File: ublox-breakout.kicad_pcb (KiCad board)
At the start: 4 copper layers, 47.2 x 33.2 mm, 41 parts, among them J1 Conn_02x06_Odd_Even, J2 Conn_Coaxial, J3 Conn_Coaxial, J4 USB_B_Micro, U1 74HCT2G125DP,125, U2 UBLOX_LEA-M8T-0, U3 TPUSBLC6-2SC6, U4 XC6206P332MR

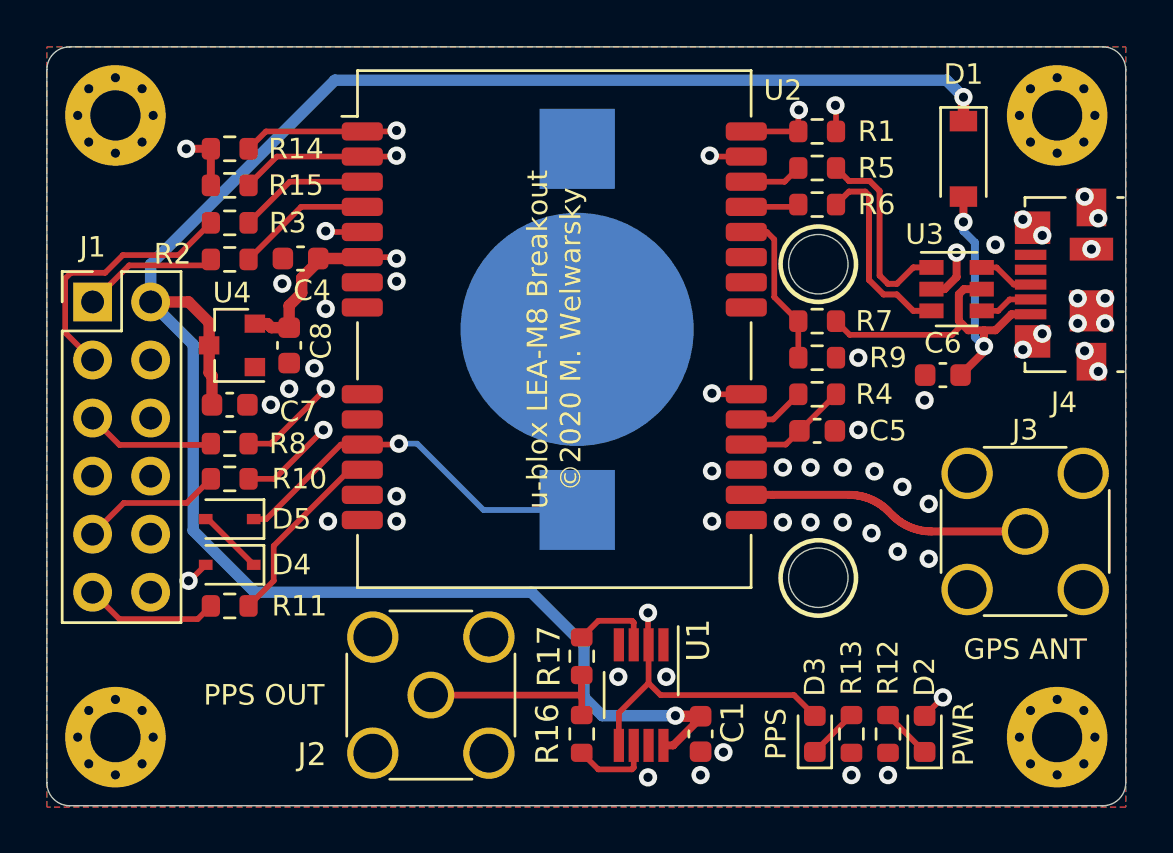
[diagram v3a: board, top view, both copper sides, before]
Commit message: PCB and schematic updates
- change backup battery circuit to prevent inverse current
- add bulk capacitor to +5V rail
- add ESD protection diode for RF input
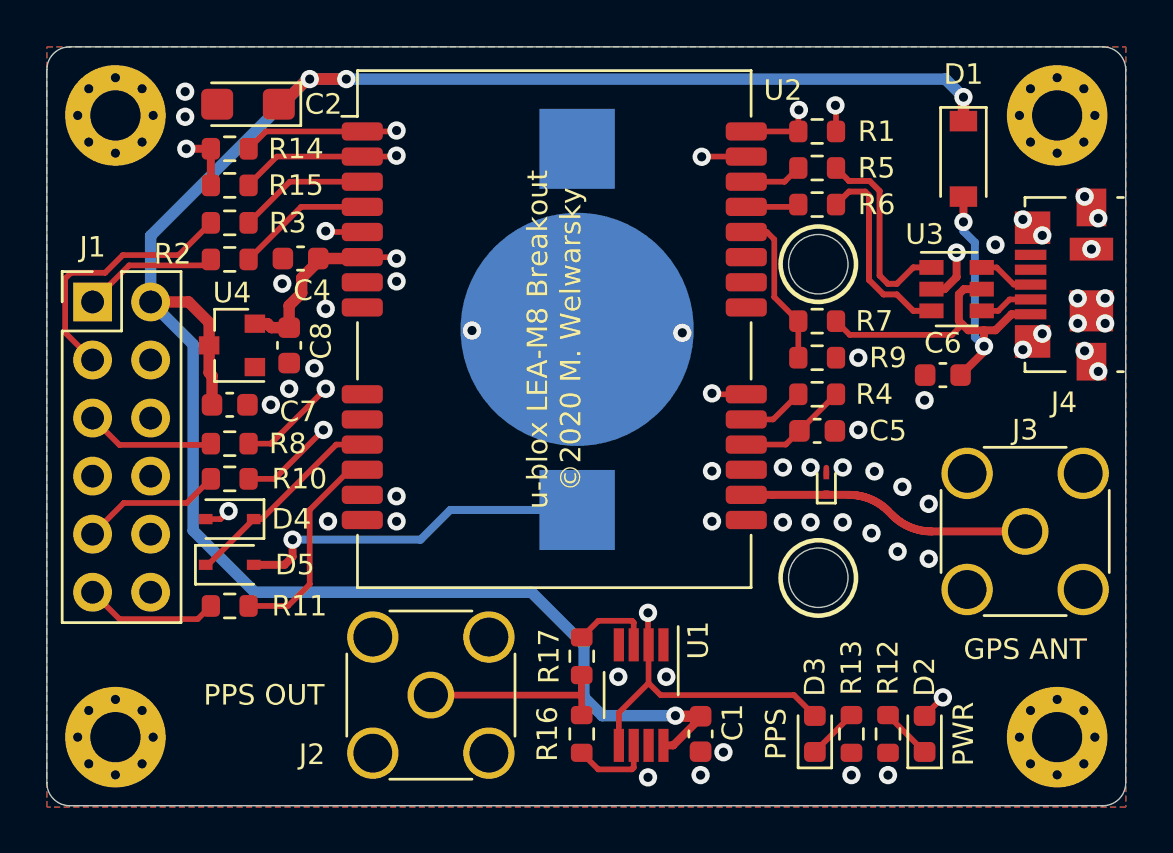
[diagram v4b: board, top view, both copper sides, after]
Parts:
- added C2: 10u, Capacitor_Tantalum_SMD:CP_EIA-3216-18_Kemet-A, F.Cu at (128.3, 100.3)
- added D6: ESD9R3.3ST5G, Diode_SMD:D_SOD-923, F.Cu at (153.6, 117.0)
- D5: value 1N4148WS -> BAT54HT1G
- moved D4 2.00 mm to (127.5, 118.5)
- moved D5 2.00 mm to (127.5, 120.5), turned to 0 degrees
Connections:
- BT1 pad 1: /V_BKP -> Net-(BT1-Pad1)
- D4 pad 1: Net-(D4-Pad1) -> /V_BKP
- D5 pad 2: Net-(D4-Pad1) -> Net-(BT1-Pad1)
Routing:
- net Net-(BT1-Pad1): track 0.00 -> 15.6 mm, vias 0 -> 1
- net /V_BKP: track 18.0 -> 9.03 mm, vias 1 -> 0
- net +5V: track 88.9 -> 93.1 mm, vias 2 -> 4
- net Net-(D4-Pad1): track 2.93 -> 0.00 mm
- net /TIMEPULSE2: track 8.34 -> 9.35 mm
- net GND: track 2.44 -> 2.77 mm, vias 48 -> 52

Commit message: Fix USB and other issues
- use an LDO to provide VDD_USB as per HIM (major issue)
- correct trace width for GPS antenna input (minor issue)
- add OSHW logo on top silk
- add copyright notice on top silk
- update gerber, BOM and CPL files
- update schematic PDF
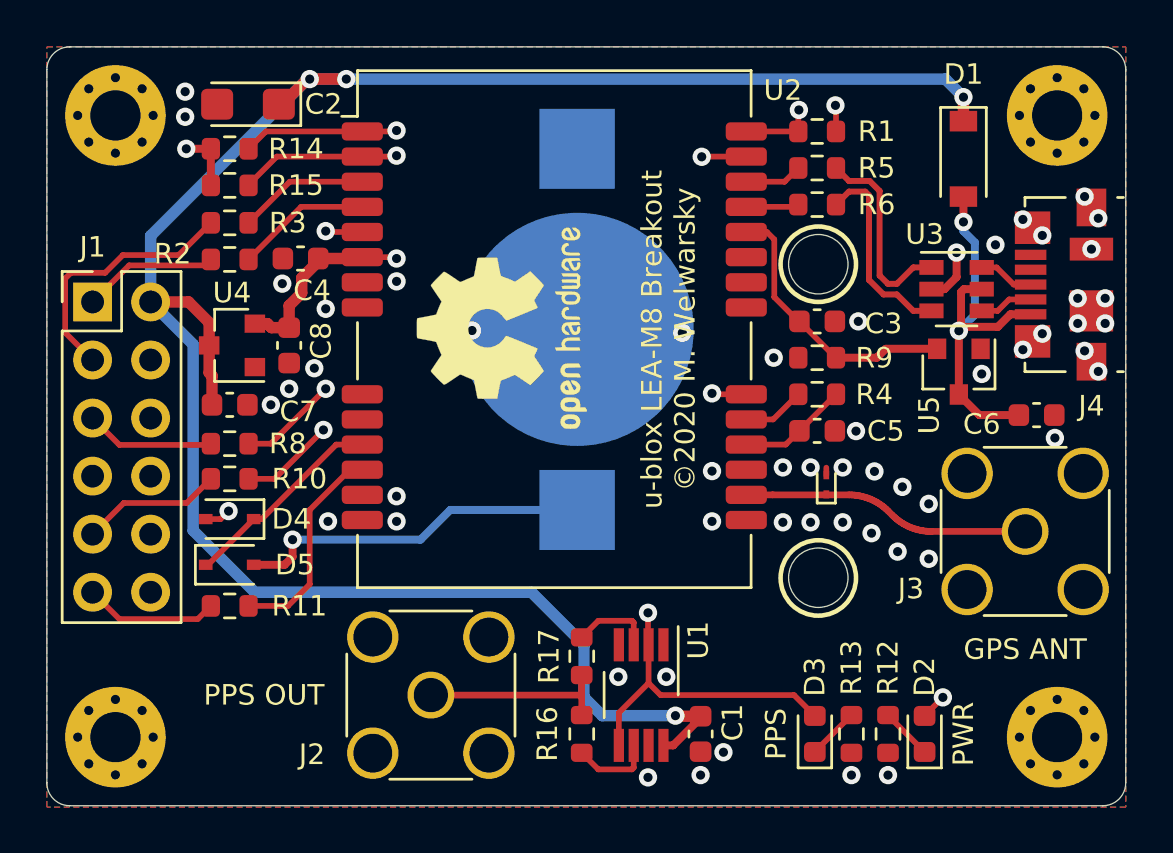
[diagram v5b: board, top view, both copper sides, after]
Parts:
- removed R7: 62k, Resistor_SMD:R_0603_1608Metric
- added C3: 1u, Capacitor_SMD:C_0603_1608Metric, F.Cu at (153.2, 109.8)
- added OSHW1: Logo_Open_Hardware_Small, Symbol:OSHW-Logo2_9.8x8mm_SilkScreen, F.Cu at (139.4, 110.1)
- added U5: XC6206P332MR, Package_TO_SOT_SMD:SOT-23, F.Cu at (159.4, 112.0)
- BT1: value Battery_Cell -> Keystone 3000
- C6: value 100n -> 1u
- R9: value 110k -> 100k
- moved C6 4.46 mm to (162.8, 113.9), turned to 0 degrees
- turned R9 to 0 degrees
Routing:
- net /VDD_USB: track 6.97 -> 12.2 mm
- net /USB_VBUS: track 21.2 -> 18.2 mm
- net GND: vias 52 -> 54
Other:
- net class 50Z: clearance 0.5842 -> 0.6

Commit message: USB updates and 1PPS updates
These changes make the USB ESD protection fully optional since the
USBLC6-2SC6 is frequently out of stock at JLCPCB
- replace USBLC6-2SC6 with USBLC6-4SC6
- route a 7mil/4mil differential pair under its body and connect it

Tighter coupling of the 74HCT2G125 buffer to the SMA connector to
bring the impedance closer to 50 Ohm
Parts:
- R16, R17: value 82 -> 68
- U3: value TPUSBLC6-2SC6 -> USBLC6-4SC6
- moved C3 4.12 mm to (156.8, 111.8), turned to 270 degrees
- moved R9 1.49 mm to (153.2, 109.9), turned to 180 degrees
- moved D1 1.02 mm to (158.6, 102.5)
- moved U5 0.20 mm to (159.4, 112.2)
- moved U3 0.15 mm to (159.4, 108.5), turned to 270 degrees
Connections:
- J4 pad 2: Net-(J4-Pad2) -> /USB_D-
- J4 pad 3: Net-(J4-Pad3) -> /USB_D+
- U3 pad 3: /USB_D- -> (no net)
- U3 pad 4: Net-(J4-Pad2) -> (no net)
- U3 pad 6: Net-(J4-Pad3) -> /USB_D-
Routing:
- net /USB_D+: track 8.74 -> 13.8 mm
- net /USB_D-: track 8.74 -> 13.7 mm
- net Net-(J4-Pad3): track 2.55 -> 0.00 mm
- net Net-(J4-Pad2): track 2.45 -> 0.00 mm
- net GND: track 2.77 -> 0.38 mm, vias 54 -> 88
- net /USB_VBUS: track 18.2 -> 19.8 mm
- net +5V: track 93.1 -> 92.0 mm
- net /VDD_USB: track 12.2 -> 13.1 mm
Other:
- net class 50Z: clearance 0.6 -> 0.65
- net class USB: clearance 0.2 -> 0.1016; trace_width 0.25 -> 0.1778
- rule trace_min: 0.2 -> 0.1016

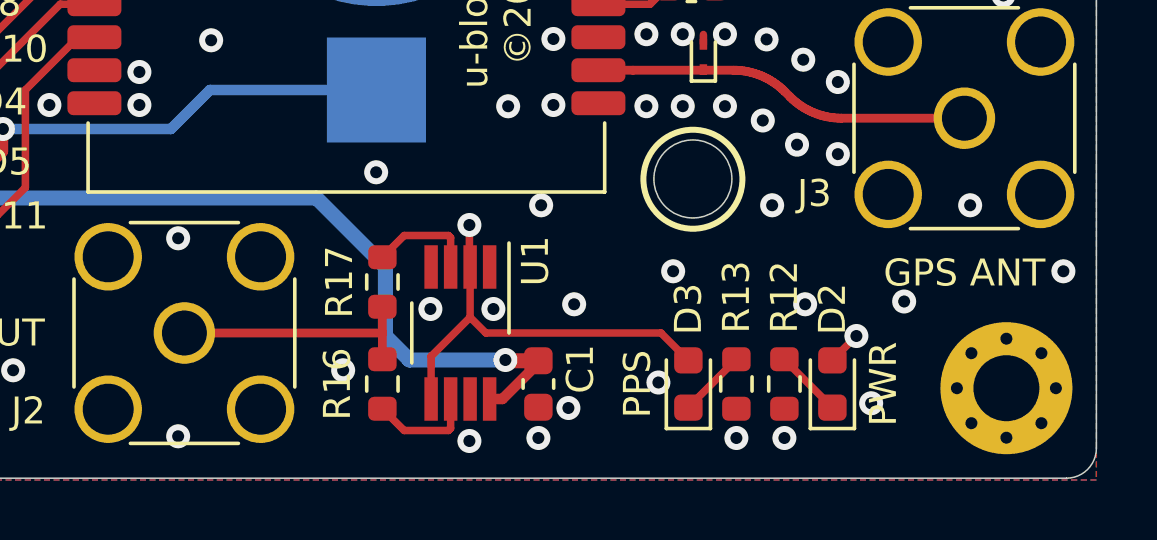
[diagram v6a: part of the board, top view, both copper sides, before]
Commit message: Update PPS output buffer
Change output buffer to 2*NC7SZ125, add a small resistor network
to lift the input signal from 3.3V LVC to standard 5V CMOS
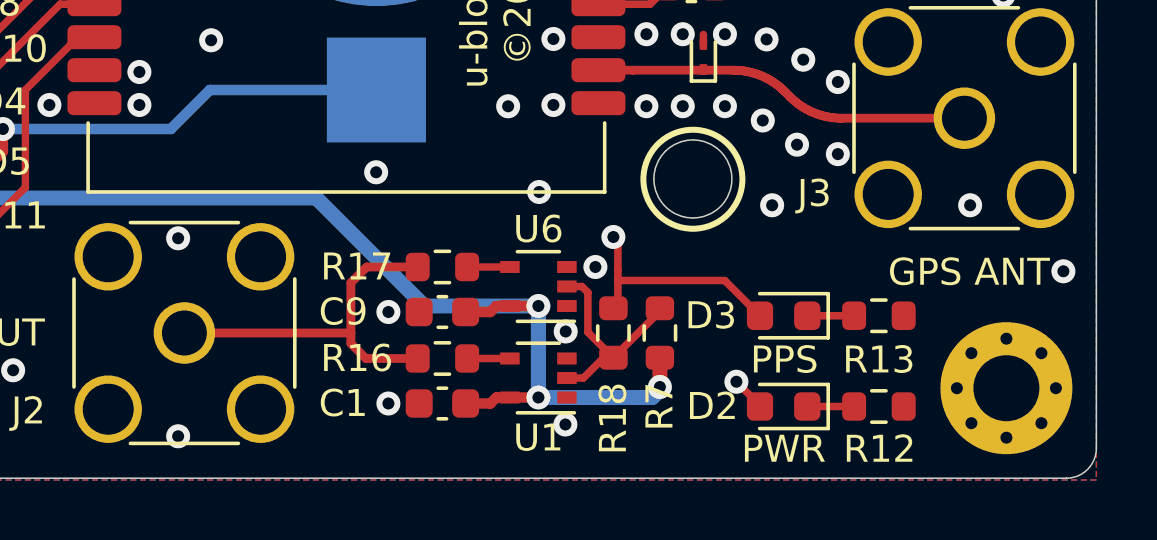
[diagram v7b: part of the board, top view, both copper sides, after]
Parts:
- added C9: 100n, Capacitor_SMD:C_0603_1608Metric, F.Cu at (144.9, 125.5)
- added R18: 680, Resistor_SMD:R_0603_1608Metric, F.Cu at (150.6, 126.2)
- added R7: 2.2k, Resistor_SMD:R_0603_1608Metric, F.Cu at (152.2, 126.2)
- added U6: 74LVC1G125, Package_TO_SOT_SMD:SOT-353_SC-70-5, F.Cu at (148.1, 124.6)
- R16, R17: value 68 -> 82
- U1: value 74HCT2G125DP,125 -> 74LVC1G125; footprint Package_SO:VSSOP-8_3.0x3.0mm_P0.65mm -> Package_TO_SOT_SMD:SOT-353_SC-70-5
- moved R13 5.27 mm to (159.4, 125.6), turned to 180 degrees
- moved D3 3.91 mm to (156.3, 125.6), turned to 180 degrees
- moved C1 3.27 mm to (144.9, 128.5), turned to 180 degrees
- moved R12 3.24 mm to (159.4, 128.6), turned to 180 degrees
- moved U1 3.00 mm to (148.1, 127.7), turned to 180 degrees
- moved R16 2.17 mm to (144.9, 127.0), turned to 0 degrees
- moved R17 2.06 mm to (144.9, 124.0), turned to 0 degrees
- moved D2 1.79 mm to (156.3, 128.6), turned to 180 degrees
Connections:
- U1 pad 2: /TIMEPULSE -> Net-(R18-Pad1)
- U1 pad 3: Net-(R17-Pad2) -> GND
- U1 pad 4: GND -> Net-(R16-Pad2)
- U1 pad 5: /TIMEPULSE -> +5V
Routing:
- net +5V: track 92.0 -> 101.0 mm, vias 4 -> 6
- net /TIMEPULSE: track 42.2 -> 34.5 mm
- net Net-(R18-Pad1): track 0.00 -> 7.43 mm
- net /PPS_OUT: track 8.35 -> 12.4 mm
- net Net-(R17-Pad2): track 3.58 -> 1.43 mm
- net Net-(R16-Pad2): track 3.58 -> 1.43 mm
- net Net-(D2-Pad1): track 2.33 -> 1.56 mm
- net Net-(D3-Pad1): track 2.28 -> 1.56 mm
- net GND: track 0.38 -> 0.33 mm, vias 88 -> 79

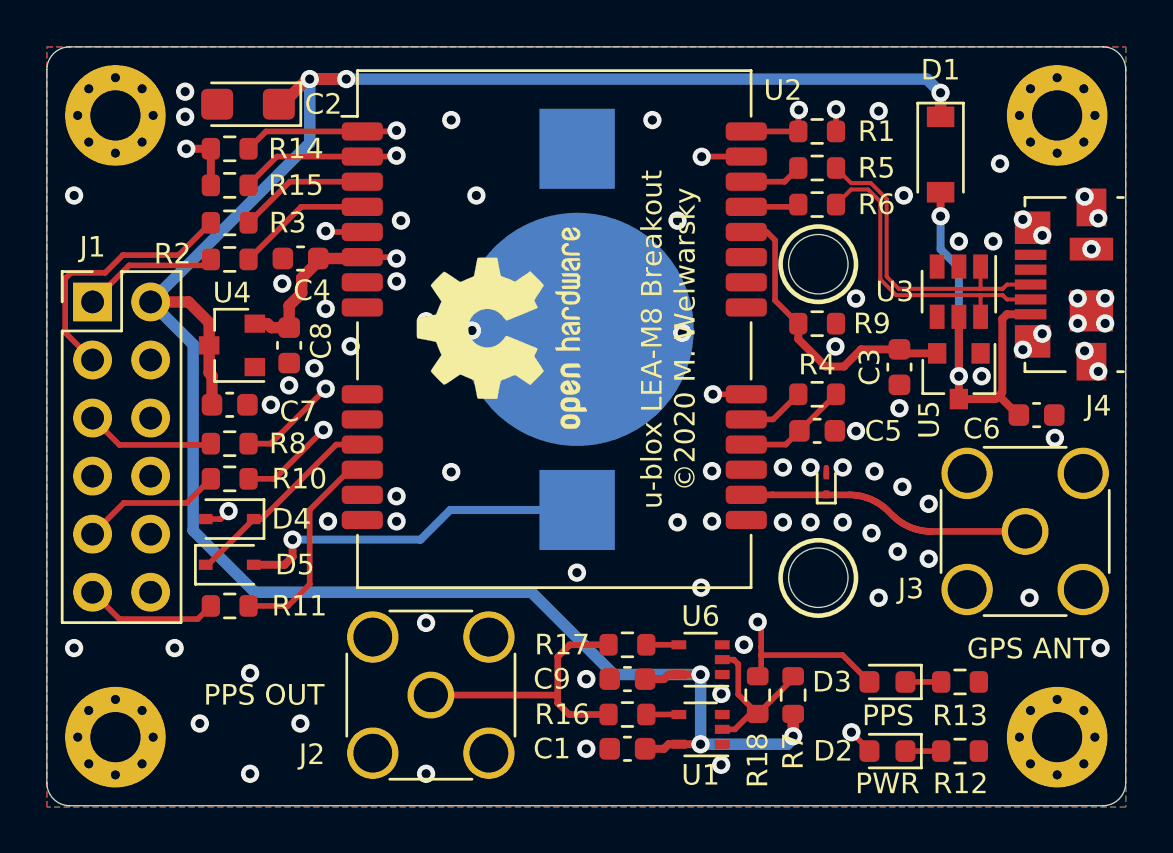
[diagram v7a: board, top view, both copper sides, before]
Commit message: Overvoltage and R.P. protection, PPS buffer updates
Added an ESD diode at the input to protect the bulk
decoupling capacitor (tantalum). It's unidirectional and provides
at least some reverse polarity protection as well (will short out).

Faster rise time at input gate of PPS buffers by adding a small
10nF capacitor

Move USB ESD protection a bit to make soldering the USB receptacle
easier
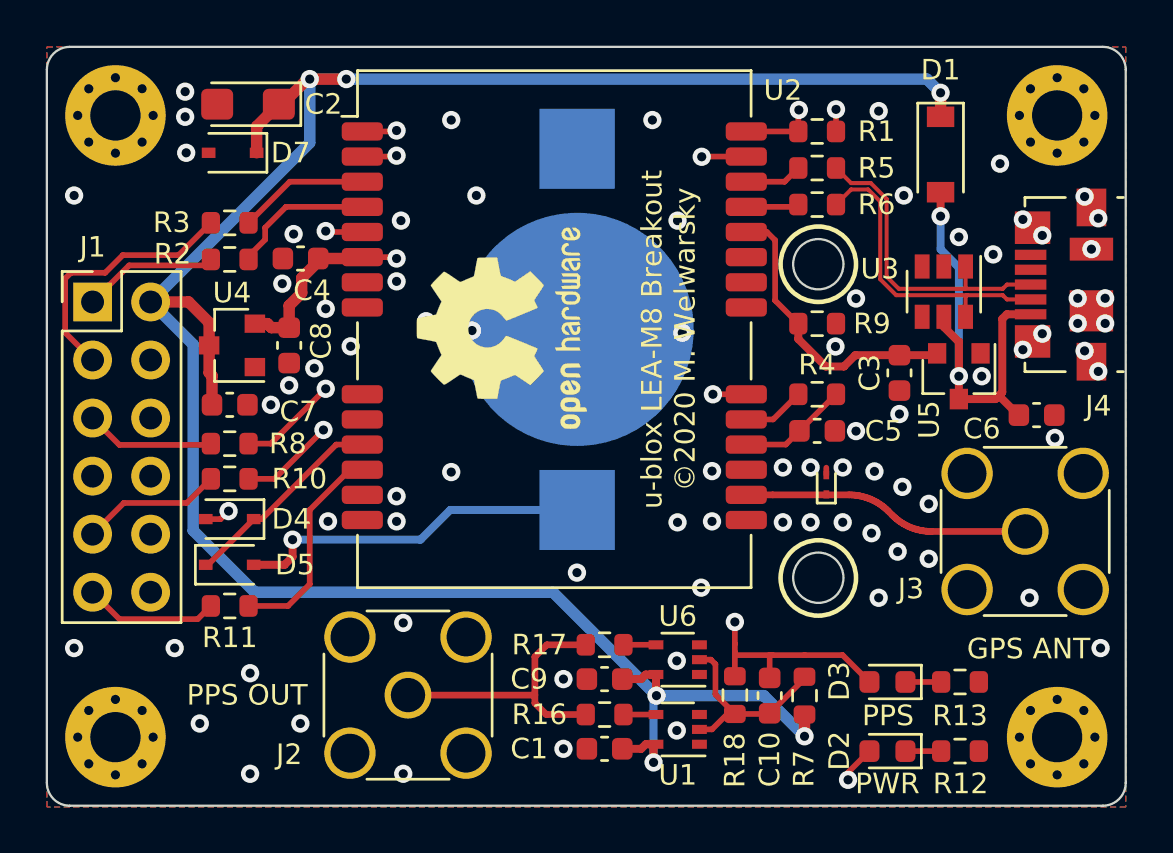
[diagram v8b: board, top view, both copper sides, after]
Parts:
- removed R14, R15: DNP, Resistor_SMD:R_0603_1608Metric
- added C10: 1n, Capacitor_SMD:C_0603_1608Metric, F.Cu at (151.1, 126.2)
- added D7: PESD5V0U1UA,115, Diode_SMD:D_SOD-323, F.Cu at (127.6, 102.4)
- R12, R13: value 620 -> 680
- R7: value 2.2k -> 2.7k
- U1, U6: value 74LVC1G125 -> NC7SZ125
- moved C1 1.00 mm to (143.9, 128.5)
- moved C9 1.00 mm to (143.9, 125.5)
- moved J2 1.00 mm to (135.3, 126.2)
- moved R16 1.00 mm to (143.9, 127.0)
- moved R17 1.00 mm to (143.9, 124.0)
- moved R18 1.00 mm to (149.6, 126.2)
- moved U1 1.00 mm to (147.1, 127.7)
- moved U6 1.00 mm to (147.1, 124.6)
- moved U3 0.66 mm to (158.7, 108.5)
- moved R7 0.50 mm to (152.6, 126.2)
- moved C3 0.25 mm to (156.8, 112.1)
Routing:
- net /SCL: track 24.0 -> 17.0 mm
- net /SDA: track 27.8 -> 21.7 mm
- net +5V: track 101.0 -> 104.7 mm
- net VDD: track 13.7 -> 11.5 mm, vias 4 -> 3
- net /TIMEPULSE: track 34.5 -> 36.5 mm
- net Net-(C10-Pad1): track 7.43 -> 8.90 mm
- net /D_SEL: track 18.5 -> 20.0 mm
- net GND: vias 79 -> 80
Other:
- outline, holes or cut-outs redrawn
